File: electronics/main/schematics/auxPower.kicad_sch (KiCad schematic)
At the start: 9 parts, among them U1 XSD366-094, U2 L7812CV-DG

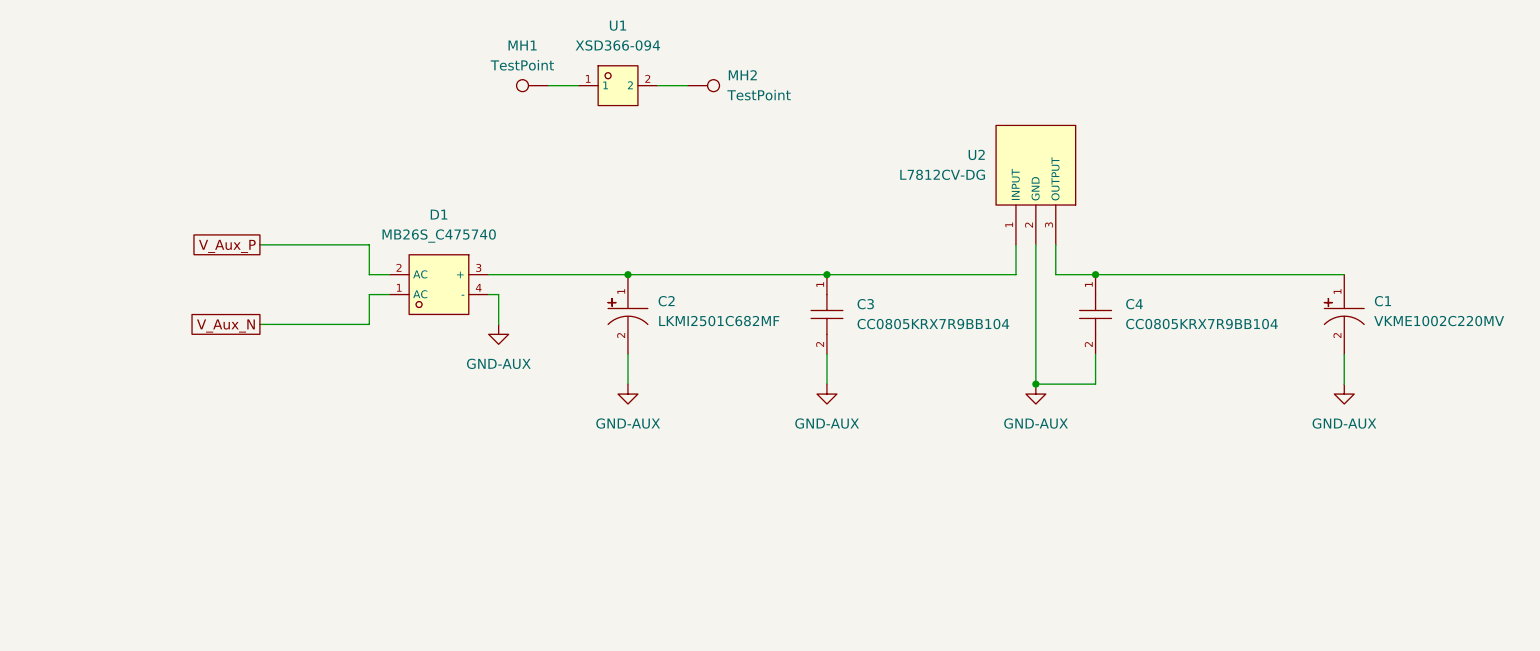
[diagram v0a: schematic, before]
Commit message: update aux voltage
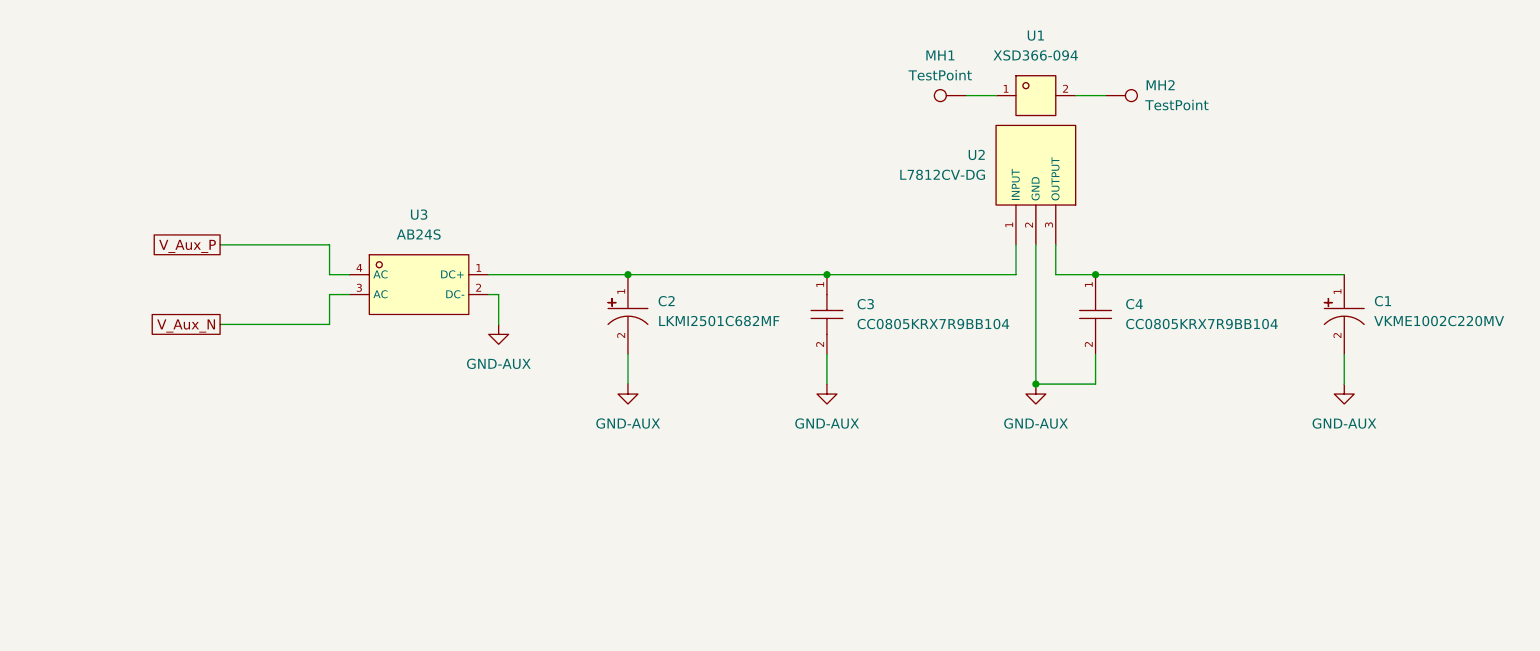
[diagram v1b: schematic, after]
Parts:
- removed D1: MB26S_C475740, footprints:MBS_L4.7-W4.0-P2.50-LS7.0-BL, symbol jlcpcb:MB26S_C475740
- added U3: AB24S, footprints:ABS-SMD_L5.0-W4.4-P4.00-LS7.0-BL, symbol jlcpcb:AB24S
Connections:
- net GND-AUX: now also U3.2 (DC-)
- net V_Aux_N: now also U3.3 (AC)
- net V_Aux_P: now also U3.4 (AC)
- net at C2.1, C3.1, U2.1 (INPUT): now also U3.1 (DC+)
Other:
- moved on the sheet: MH1, MH2
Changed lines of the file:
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@@
 	(wire
 		(pts
-			(xy 71.12 93.98) (xy 57.15 93.98)
-		)
-		(stroke
-			(width 0)
-			(type default)
-		)
-	)
-	(wire
-		(pts
-			(xy 73.66 90.17) (xy 71.12 90.17)
+			(xy 66.04 93.98) (xy 52.07 93.98)
+		)
+		(stroke
+			(width 0)
+			(type default)
+		)
+	)
+	(wire
+		(pts
+			(xy 68.58 90.17) (xy 66.04 90.17)
 		)
 		(stroke
@@
 	(wire
 		(pts
-			(xy 107.95 63.5) (xy 111.76 63.5)
-		)
-		(stroke
-			(width 0)
-			(type default)
-		)
-	)
-	(wire
-		(pts
-			(xy 93.98 63.5) (xy 97.79 63.5)
-		)
-		(stroke
-			(width 0)
-			(type default)
-		)
-	)
-	(wire
-		(pts
-			(xy 71.12 83.82) (xy 71.12 87.63)
-		)
-		(stroke
-			(width 0)
-			(type default)
-		)
-	)
-	(wire
-		(pts
-			(xy 71.12 90.17) (xy 71.12 93.98)
+			(xy 161.29 64.77) (xy 165.1 64.77)
+		)
+		(stroke
+			(width 0)
+			(type default)
+		)
+	)
+	(wire
+		(pts
+			(xy 147.32 64.77) (xy 151.13 64.77)
+		)
+		(stroke
+			(width 0)
+			(type default)
+		)
+	)
+	(wire
+		(pts
+			(xy 66.04 83.82) (xy 66.04 87.63)
+		)
+		(stroke
+			(width 0)
+			(type default)
+		)
+	)
+	(wire
+		(pts
+			(xy 66.04 90.17) (xy 66.04 93.98)
 		)
 		(stroke
@@
 	(wire
 		(pts
-			(xy 57.15 83.82) (xy 71.12 83.82)
+			(xy 52.07 83.82) (xy 66.04 83.82)
 		)
 		(stroke
@@
 	(wire
 		(pts
-			(xy 71.12 87.63) (xy 73.66 87.63)
+			(xy 66.04 87.63) (xy 68.58 87.63)
 		)
 		(stroke
@@
 	(global_label "V_Aux_P"
 		(shape passive)
-		(at 57.15 83.82 180)
+		(at 52.07 83.82 180)
 		(fields_autoplaced yes)
 		(effects
@@
 		)
 		(property "Intersheetrefs" "${INTERSHEET_REFS}"
-			(at 47.7166 83.82 0)
+			(at 42.6366 83.82 0)
 			(effects
 				(font
@@
 	(global_label "V_Aux_N"
 		(shape passive)
-		(at 57.15 93.98 180)
+		(at 52.07 93.98 180)
 		(fields_autoplaced yes)
 		(effects
@@
 		)
 		(property "Intersheetrefs" "${INTERSHEET_REFS}"
-			(at 47.6561 93.98 0)
+			(at 42.5761 93.98 0)
 			(effects
 				(font
@@
 				(justify right)
 				(hide yes)
-			)
-		)
-	)
-	(symbol
-		(lib_id "jlcpcb:MB26S_C475740")
-		(at 80.01 88.9 0)
-		(mirror y)
-		(unit 1)
-		(exclude_from_sim no)
-		(in_bom yes)
-		(on_board yes)
-		(dnp no)
-		(property "Reference" "D1"
-			(at 80.01 80.01 0)
-			(effects
-				(font
-					(size 1.27 1.27)
-				)
-			)
-		)
-		(property "Value" "MB26S_C475740"
-			(at 80.01 82.55 0)
-			(effects
-				(font
-					(size 1.27 1.27)
-				)
-			)
-		)
-		(property "Footprint" "footprints:MBS_L4.7-W4.0-P2.50-LS7.0-BL"
-			(at 80.01 99.06 0)
-			(effects
-				(font
-					(size 1.27 1.27)
-					(italic yes)
-				)
-				(hide yes)
-			)
-		)
-		(property "Datasheet" "https://item.szlcsc.com/335287.html"
-			(at 82.296 88.773 0)
-			(effects
-				(font
-					(size 1.27 1.27)
-				)
-				(justify left)
-				(hide yes)
-			)
-		)
-		(property "Description" ""
-			(at 80.01 88.9 0)
-			(effects
-				(font
-					(size 1.27 1.27)
-				)
-				(hide yes)
-			)
-		)
-		(property "LCSC" "C475740"
-			(at 80.01 88.9 0)
-			(effects
-				(font
-					(size 1.27 1.27)
-				)
-				(hide yes)
-			)
-		)
-		(pin "1"
-		)
-		(pin "2"
-		)
-		(pin "3"
-		)
-		(pin "4"
-		)
-		(instances
-			(project ""
-				(path "/6805e3ef-87bd-473d-890f-05ae2da73c1a/c06d43ef-ca8e-4531-a839-7ed47019a243"
-					(reference "D1")
-					(unit 1)
-				)
 			)
 		)
@@
 	(symbol
 		(lib_id "Connector:TestPoint")
-		(at 93.98 63.5 90)
+		(at 147.32 64.77 90)
 		(unit 1)
 		(exclude_from_sim no)
@@
 		(fields_autoplaced yes)
 		(property "Reference" "MH1"
-			(at 90.678 58.42 90)
+			(at 144.018 59.69 90)
 			(effects
 				(font
@@
 		)
 		(property "Value" "TestPoint"
-			(at 90.678 60.96 90)
+			(at 144.018 62.23 90)
 			(effects
 				(font
@@
 		)
 		(property "Footprint" "MountingHole:MountingHole_2.2mm_M2_DIN965_Pad_TopBottom"
-			(at 93.98 58.42 0)
+			(at 147.32 59.69 0)
 			(effects
 				(font
@@
 		)
 		(property "Datasheet" "~"
-			(at 93.98 58.42 0)
+			(at 147.32 59.69 0)
 			(effects
 				(font
@@
 		)
 		(property "Description" "test point"
-			(at 93.98 63.5 0)
+			(at 147.32 64.77 0)
 			(effects
 				(font
@@
 	)
 	(symbol
+		(lib_id "jlcpcb:AB24S")
+		(at 77.47 88.9 0)
+		(unit 1)
+		(exclude_from_sim no)
+		(in_bom yes)
+		(on_board yes)
+		(dnp no)
+		(fields_autoplaced yes)
+		(property "Reference" "U3"
+			(at 77.47 80.01 0)
+			(effects
+				(font
+					(size 1.27 1.27)
+				)
+			)
+		)
+		(property "Value" "AB24S"
+			(at 77.47 82.55 0)
+			(effects
+				(font
+					(size 1.27 1.27)
+				)
+			)
+		)
+		(property "Footprint" "footprints:ABS-SMD_L5.0-W4.4-P4.00-LS7.0-BL"
+			(at 77.47 99.06 0)
+			(effects
+				(font
+					(size 1.27 1.27)
+					(italic yes)
+				)
+				(hide yes)
+			)
+		)
+		(property "Datasheet" "https://atta.szlcsc.com/upload/public/pdf/source/20211116/1CFCA0CE490D28CCD798815519BDD3FD.pdf"
+			(at 75.184 88.773 0)
+			(effects
+				(font
+					(size 1.27 1.27)
+				)
+				(justify left)
+				(hide yes)
+			)
+		)
+		(property "Description" ""
+			(at 77.47 88.9 0)
+			(effects
+				(font
+					(size 1.27 1.27)
+				)
+				(hide yes)
+			)
+		)
+		(property "LCSC" "C882375"
+			(at 77.47 88.9 0)
+			(effects
+				(font
+					(size 1.27 1.27)
+				)
+				(hide yes)
+			)
+		)
+		(pin "1"
+		)
+		(pin "3"
+		)
+		(pin "2"
+		)
+		(pin "4"
+		)
+		(instances
+			(project ""
+				(path "/6805e3ef-87bd-473d-890f-05ae2da73c1a/c06d43ef-ca8e-4531-a839-7ed47019a243"
+					(reference "U3")
+					(unit 1)
+				)
+			)
+		)
+	)
+	(symbol
 		(lib_id "jlcpcb:XSD366-094")
-		(at 102.87 63.5 0)
+		(at 156.21 64.77 0)
 		(unit 1)
 		(exclude_from_sim no)
@@
 		(fields_autoplaced yes)
 		(property "Reference" "U1"
-			(at 102.87 55.88 0)
+			(at 156.21 57.15 0)
 			(effects
 				(font
@@
 		)
 		(property "Value" "XSD366-094"
-			(at 102.87 58.42 0)
+			(at 156.21 59.69 0)
 			(effects
 				(font
@@
 		)
 		(property "Footprint" "footprints:HEATSINK-TH_XSD366-094"
-			(at 102.87 73.66 0)
+			(at 156.21 74.93 0)
 			(effects
 				(font
@@
 		)
 		(property "Datasheet" "https://atta.szlcsc.com/upload/public/pdf/source/20180927/C286227_8CAF4AF643AF3F6953ADE6744A76F022.pdf"
-			(at 100.584 63.373 0)
+			(at 153.924 64.643 0)
 			(effects
 				(font
@@
 		)
 		(property "Description" ""
-			(at 102.87 63.5 0)
+			(at 156.21 64.77 0)
 			(effects
 				(font
@@
 		)
 		(property "LCSC" "C286227"
-			(at 102.87 63.5 0)
+			(at 156.21 64.77 0)
 			(effects
 				(font
@@
 	(symbol
 		(lib_id "Connector:TestPoint")
-		(at 111.76 63.5 270)
+		(at 165.1 64.77 270)
 		(unit 1)
 		(exclude_from_sim no)
@@
 		(fields_autoplaced yes)
 		(property "Reference" "MH2"
-			(at 116.84 62.2299 90)
+			(at 170.18 63.4999 90)
 			(effects
 				(font
@@
 		)
 		(property "Value" "TestPoint"
-			(at 116.84 64.7699 90)
+			(at 170.18 66.0399 90)
 			(effects
 				(font
@@
 		)
 		(property "Footprint" "MountingHole:MountingHole_2.2mm_M2_DIN965_Pad_TopBottom"
-			(at 111.76 68.58 0)
+			(at 165.1 69.85 0)
 			(effects
 				(font
@@
 		)
 		(property "Datasheet" "~"
-			(at 111.76 68.58 0)
+			(at 165.1 69.85 0)
 			(effects
 				(font
@@
 		)
 		(property "Description" "test point"
-			(at 111.76 63.5 0)
-			(effects
-				(font
+			(at 165.1 64.77 0)
+			(effects
+				(font

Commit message: widerstände angelegt
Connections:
- net +12V: now reaches C1.1, C4.1, U2.3 (OUTPUT)
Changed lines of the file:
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@@
+	)
+	(junction
+		(at 195.58 87.63)
+		(diameter 0)
+		(color 0 0 0 0)
 	)
 	(junction
@@
 	(wire
 		(pts
+			(xy 212.09 78.74) (xy 212.09 87.63)
+		)
+		(stroke
+			(width 0)
+			(type default)
+		)
+	)
+	(wire
+		(pts
 			(xy 52.07 83.82) (xy 66.04 83.82)
 		)
@@
 		(pts
 			(xy 195.58 97.79) (xy 195.58 101.6)
+		)
+		(stroke
+			(width 0)
+			(type default)
+		)
+	)
+	(wire
+		(pts
+			(xy 212.09 87.63) (xy 195.58 87.63)
 		)
 		(stroke
@@
 					(unit 1)
 				)
+			)
+		)
+	)
+	(symbol
+		(lib_id "power:+12V")
+		(at 212.09 78.74 0)
+		(unit 1)
+		(exclude_from_sim no)
+		(in_bom yes)
+		(on_board yes)
+		(dnp no)
+		(fields_autoplaced yes)
+		(property "Reference" "#PWR06"
+			(at 212.09 82.55 0)
+			(effects
+				(font
+					(size 1.27 1.27)
+				)
+				(hide yes)
+			)
+		)
+		(property "Value" "+12V"
+			(at 212.09 73.66 0)
+			(effects
+				(font
+					(size 1.27 1.27)
+				)
+			)
+		)
+		(property "Footprint" ""
+			(at 212.09 78.74 0)
+			(effects
+				(font
+					(size 1.27 1.27)
+				)
+				(hide yes)
+			)
+		)
+		(property "Datasheet" ""
+			(at 212.09 78.74 0)
+			(effects
+				(font
+					(size 1.27 1.27)
+				)
+				(hide yes)
+			)
+		)
+		(property "Description" "Power symbol creates a global label with name \"+12V\""
+			(at 212.09 78.74 0)
+			(effects
+				(font
+					(size 1.27 1.27)
+				)
+				(hide yes)
+			)
+		)
+		(pin "1"
+		)
+		(instances
+			(project ""
+				(path "/6805e3ef-87bd-473d-890f-05ae2da73c1a/c06d43ef-ca8e-4531-a839-7ed47019a243"
+					(reference "#PWR06")
+					(unit 1)
+				)

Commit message: schematic ready? - check
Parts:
- removed C1: VKME1002C220MV, footprints:CAP-SMD_BD10.0-L10.3-W10.3-LS11.7-FD, symbol jlcpcb:VKME1002C220MV
- added AC-IN4, AC-IN5: 1, TestPoint:TestPoint_THTPad_D2.0mm_Drill1.0mm, symbol Connector:TestPoint_Small
- added C1: 33uF 50V, footprints:CAP-TH_BD5.0-P2.00-D0.8-FD, symbol jlcpcb:KM330M050C110A
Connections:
- net +12V: now also C1.1
- net GND-AUX: now also C1.2
- net V_Aux_N: no longer names the net of U3.3 (AC)
- net V_Aux_N: now also AC-IN5.1
- net V_Aux_P: no longer names the net of U3.4 (AC)
- net V_Aux_P: now also AC-IN4.1
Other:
- note added: "12,6 V ~"

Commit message: updated PCB
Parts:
- added N1: ~, wb50_footprints:NetTie_0.5mm_2Pad, symbol wb50_symbols:NetTie
- AC-IN4, AC-IN5: footprint TestPoint:TestPoint_THTPad_D2.0mm_Drill1.0mm -> TestPoint:TestPoint_THTPad_D3.0mm_Drill1.5mm
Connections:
- net GND-AUX: now also N1.2 (Net2)
- new net GND-PWR: N1.1 (Net1)
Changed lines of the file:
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@@
+	(wire
+		(pts
+			(xy 146.05 128.27) (xy 146.05 125.73)
+		)
+		(stroke
+			(width 0)
+			(type default)
+		)
+	)
+	(wire
+		(pts
+			(xy 133.35 125.73) (xy 133.35 128.27)
+		)
+		(stroke
+			(width 0)
+			(type default)
+		)
+	)
 	(wire
 		(pts
@@
 	(wire
 		(pts
-			(xy 158.75 87.63) (xy 163.83 87.63)
+			(xy 135.89 125.73) (xy 133.35 125.73)
 		)
 		(stroke
@@
 	(wire
 		(pts
-			(xy 163.83 87.63) (xy 195.58 87.63)
+			(xy 158.75 87.63) (xy 163.83 87.63)
 		)
 		(stroke
@@
 		)
 	)
+	(wire
+		(pts
+			(xy 163.83 87.63) (xy 195.58 87.63)
+		)
+		(stroke
+			(width 0)
+			(type default)
+		)
+	)
+	(wire
+		(pts
+			(xy 146.05 125.73) (xy 140.97 125.73)
+		)
+		(stroke
+			(width 0)
+			(type default)
+		)
+	)
 	(symbol
 		(lib_id "power:GND")
@@
 				(path "/6805e3ef-87bd-473d-890f-05ae2da73c1a/c06d43ef-ca8e-4531-a839-7ed47019a243"
 					(reference "#PWR02")
+					(unit 1)
+				)
+			)
+		)
+	)
+	(symbol
+		(lib_id "power:GND")
+		(at 133.35 128.27 0)
+		(unit 1)
+		(exclude_from_sim no)
+		(in_bom yes)
+		(on_board yes)
+		(dnp no)
+		(property "Reference" "#PWR045"
+			(at 133.35 134.62 0)
+			(effects
+				(font
+					(size 1.27 1.27)
+				)
+				(hide yes)
+			)
+		)
+		(property "Value" "GND-AUX"
+			(at 133.35 132.334 0)
+			(effects
+				(font
+					(size 1.27 1.27)
+				)
+			)
+		)
+		(property "Footprint" ""
+			(at 133.35 128.27 0)
+			(effects
+				(font
+					(size 1.27 1.27)
+				)
+				(hide yes)
+			)
+		)
+		(property "Datasheet" ""
+			(at 133.35 128.27 0)
+			(effects
+				(font
+					(size 1.27 1.27)
+				)
+				(hide yes)
+			)
+		)
+		(property "Description" "Power symbol creates a global label with name \"GND\" , ground"
+			(at 133.35 128.27 0)
+			(effects
+				(font
+					(size 1.27 1.27)
+				)
+				(hide yes)
+			)
+		)
+		(pin "1"
+		)
+		(instances
+			(project "wb50"
+				(path "/6805e3ef-87bd-473d-890f-05ae2da73c1a/c06d43ef-ca8e-4531-a839-7ed47019a243"
+					(reference "#PWR045")
 					(unit 1)
 				)
@@
 			)
 		)
-		(property "Footprint" "TestPoint:TestPoint_THTPad_D2.0mm_Drill1.0mm"
+		(property "Footprint" "TestPoint:TestPoint_THTPad_D3.0mm_Drill1.5mm"
 			(at 38.1 93.98 0)
 			(effects
@@
 	)
 	(symbol
+		(lib_id "power:GND")
+		(at 146.05 128.27 0)
+		(unit 1)
+		(exclude_from_sim no)
+		(in_bom yes)
+		(on_board yes)
+		(dnp no)
+		(property "Reference" "#PWR046"
+			(at 146.05 134.62 0)
+			(effects
+				(font
+					(size 1.27 1.27)
+				)
+				(hide yes)
+			)
+		)
+		(property "Value" "GND-PWR"
+			(at 146.05 132.334 0)
+			(effects
+				(font
+					(size 1.27 1.27)
+				)
+			)
+		)
+		(property "Footprint" ""
+			(at 146.05 128.27 0)
+			(effects
+				(font
+					(size 1.27 1.27)
+				)
+				(hide yes)
+			)
+		)
+		(property "Datasheet" ""
+			(at 146.05 128.27 0)
+			(effects
+				(font
+					(size 1.27 1.27)
+				)
+				(hide yes)
+			)
+		)
+		(property "Description" "Power symbol creates a global label with name \"GND\" , ground"
+			(at 146.05 128.27 0)
+			(effects
+				(font
+					(size 1.27 1.27)
+				)
+				(hide yes)
+			)
+		)
+		(pin "1"
+		)
+		(instances
+			(project "wb50"
+				(path "/6805e3ef-87bd-473d-890f-05ae2da73c1a/c06d43ef-ca8e-4531-a839-7ed47019a243"
+					(reference "#PWR046")
+					(unit 1)
+				)
+			)
+		)
+	)
+	(symbol
+		(lib_id "wb50_symbols:NetTie")
+		(at 138.43 125.73 0)
+		(unit 1)
+		(exclude_from_sim no)
+		(in_bom yes)
+		(on_board yes)
+		(dnp no)
+		(fields_autoplaced yes)
+		(property "Reference" "N1"
+			(at 138.43 120.65 0)
+			(effects
+				(font
+					(size 1.27 1.27)
+				)
+			)
+		)
+		(property "Value" "~"
+			(at 138.43 123.19 0)
+			(effects
+				(font
+					(size 1.27 1.27)
+				)
+			)
+		)
+		(property "Footprint" "wb50_footprints:NetTie_0.5mm_2Pad"
+			(at 138.43 125.73 0)
+			(effects
+				(font
+					(size 1.27 1.27)
+				)
+				(hide yes)
+			)
+		)
+		(property "Datasheet" ""
+			(at 138.43 125.73 0)
+			(effects
+				(font
+					(size 1.27 1.27)
+				)
+				(hide yes)
+			)
+		)
+		(property "Description" ""
+			(at 138.43 125.73 0)
+			(effects
+				(font
+					(size 1.27 1.27)
+				)
+				(hide yes)
+			)
+		)
+		(pin "2"
+		)
+		(pin "1"
+		)
+		(instances
+			(project ""
+				(path "/6805e3ef-87bd-473d-890f-05ae2da73c1a/c06d43ef-ca8e-4531-a839-7ed47019a243"
+					(reference "N1")
+					(unit 1)
+				)
+			)
+		)
+	)
+	(symbol
 		(lib_id "power:+12V")
 		(at 212.09 78.74 0)
@@
 			)
 		)
-		(property "Footprint" "TestPoint:TestPoint_THTPad_D2.0mm_Drill1.0mm"
+		(property "Footprint" "TestPoint:TestPoint_THTPad_D3.0mm_Drill1.5mm"
 			(at 38.1 83.82 0)
 			(effects

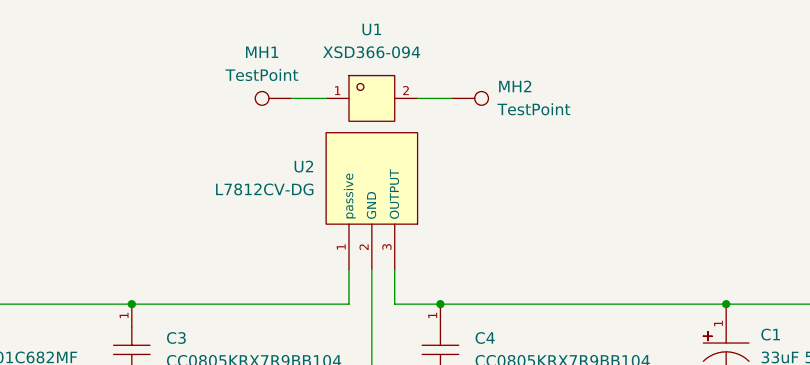
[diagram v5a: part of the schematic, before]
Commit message: update housing, speakers and schematics
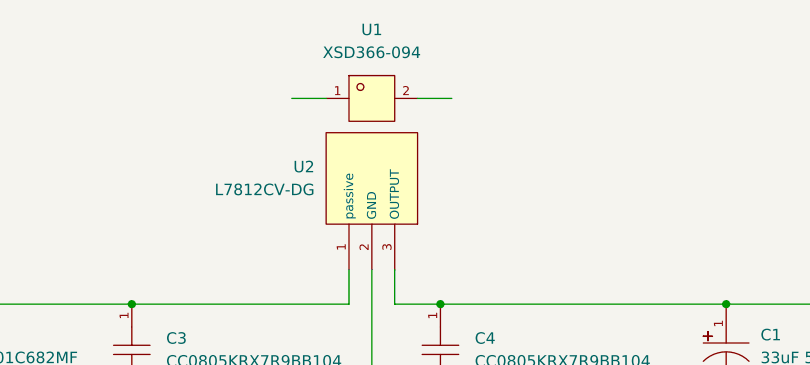
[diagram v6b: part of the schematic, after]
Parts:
- removed MH1, MH2: TestPoint, MountingHole:MountingHole_2.2mm_M2_DIN965_Pad_TopBottom, symbol Connector:TestPoint
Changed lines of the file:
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@@
-	)
-	(symbol
-		(lib_id "Connector:TestPoint")
-		(at 147.32 64.77 90)
-		(unit 1)
-		(exclude_from_sim no)
-		(in_bom yes)
-		(on_board yes)
-		(dnp no)
-		(fields_autoplaced yes)
-		(property "Reference" "MH1"
-			(at 144.018 59.69 90)
-			(effects
-				(font
-					(size 1.27 1.27)
-				)
-			)
-		)
-		(property "Value" "TestPoint"
-			(at 144.018 62.23 90)
-			(effects
-				(font
-					(size 1.27 1.27)
-				)
-			)
-		)
-		(property "Footprint" "MountingHole:MountingHole_2.2mm_M2_DIN965_Pad_TopBottom"
-			(at 147.32 59.69 0)
-			(effects
-				(font
-					(size 1.27 1.27)
-				)
-				(hide yes)
-			)
-		)
-		(property "Datasheet" "~"
-			(at 147.32 59.69 0)
-			(effects
-				(font
-					(size 1.27 1.27)
-				)
-				(hide yes)
-			)
-		)
-		(property "Description" "test point"
-			(at 147.32 64.77 0)
-			(effects
-				(font
-					(size 1.27 1.27)
-				)
-				(hide yes)
-			)
-		)
-		(pin "1"
-		)
-		(instances
-			(project ""
-				(path "/6805e3ef-87bd-473d-890f-05ae2da73c1a/c06d43ef-ca8e-4531-a839-7ed47019a243"
-					(reference "MH1")
-					(unit 1)
-				)
-			)
-		)
 	)
 	(symbol
@@
 					(unit 1)
 				)
-			)
-		)
-	)
-	(symbol
-		(lib_id "Connector:TestPoint")
-		(at 165.1 64.77 270)
-		(unit 1)
-		(exclude_from_sim no)
-		(in_bom yes)
-		(on_board yes)
-		(dnp no)
-		(fields_autoplaced yes)
-		(property "Reference" "MH2"
-			(at 170.18 63.4999 90)
-			(effects
-				(font
-					(size 1.27 1.27)
-				)
-				(justify left)
-			)
-		)
-		(property "Value" "TestPoint"
-			(at 170.18 66.0399 90)
-			(effects
-				(font
-					(size 1.27 1.27)
-				)
-				(justify left)
-			)
-		)
-		(property "Footprint" "MountingHole:MountingHole_2.2mm_M2_DIN965_Pad_TopBottom"
-			(at 165.1 69.85 0)
-			(effects
-				(font
-					(size 1.27 1.27)
-				)
-				(hide yes)
-			)
-		)
-		(property "Datasheet" "~"
-			(at 165.1 69.85 0)
-			(effects
-				(font
-					(size 1.27 1.27)
-				)
-				(hide yes)
-			)
-		)
-		(property "Description" "test point"
-			(at 165.1 64.77 0)
-			(effects
-				(font
-					(size 1.27 1.27)
-				)
-				(hide yes)
-			)
-		)
-		(pin "1"
-		)
-		(instances
-			(project "wb50"
-				(path "/6805e3ef-87bd-473d-890f-05ae2da73c1a/c06d43ef-ca8e-4531-a839-7ed47019a243"
-					(reference "MH2")
-					(unit 1)
-				)
